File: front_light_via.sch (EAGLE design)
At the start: 9 parts

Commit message: via gerbers generated
via boards completed and gerbers generated
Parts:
- renumbered ETH1 to FRONT, L_DRIVE to BLINK_R, L_SIG to DRIVING_L, R-DRIVE to BLINK_L, R_SIG to DRIVING_R
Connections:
- net N$2 renamed BLINK_L
- net N$4 renamed BLIINK_R
- net N$6 renamed DRIVING_R
- net N$8 renamed DRIVING_L
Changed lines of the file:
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@@
 <?xml version="1.0" encoding="utf-8"?>
 <!DOCTYPE eagle SYSTEM "eagle.dtd">
-<eagle version="8.3.1">
+<eagle version="8.6.0">
 <drawing>
 <settings>
@@
 </classes>
 <parts>
-<part name="ETH1" library="ETHERNET" deviceset="ETHERNET" device=""/>
-<part name="L_SIG" library="TE 2-pin connector" deviceset="2_PIN_TECONNECTOR" device=""/>
-<part name="R_SIG" library="TE 2-pin connector" deviceset="2_PIN_TECONNECTOR" device=""/>
-<part name="L_DRIVE" library="TE 2-pin connector" deviceset="2_PIN_TECONNECTOR" device=""/>
-<part name="R-DRIVE" library="TE 2-pin connector" deviceset="2_PIN_TECONNECTOR" device=""/>
+<part name="FRONT" library="ETHERNET" deviceset="ETHERNET" device=""/>
+<part name="DRIVING_L" library="TE 2-pin connector" deviceset="2_PIN_TECONNECTOR" device=""/>
+<part name="DRIVING_R" library="TE 2-pin connector" deviceset="2_PIN_TECONNECTOR" device=""/>
+<part name="BLINK_R" library="TE 2-pin connector" deviceset="2_PIN_TECONNECTOR" device=""/>
+<part name="BLINK_L" library="TE 2-pin connector" deviceset="2_PIN_TECONNECTOR" device=""/>
 <part name="H1" library="SparkFun-Electromechanical" deviceset="STAND-OFF" device=""/>
 <part name="H2" library="SparkFun-Electromechanical" deviceset="STAND-OFF" device=""/>
@@
 </plain>
 <instances>
-<instance part="ETH1" gate="G$1" x="48.26" y="68.58" rot="R180"/>
-<instance part="L_SIG" gate="G$1" x="116.84" y="88.9"/>
-<instance part="R_SIG" gate="G$1" x="119.38" y="68.58"/>
-<instance part="L_DRIVE" gate="G$1" x="119.38" y="50.8"/>
-<instance part="R-DRIVE" gate="G$1" x="119.38" y="30.48"/>
+<instance part="FRONT" gate="G$1" x="48.26" y="68.58" rot="R180"/>
+<instance part="DRIVING_L" gate="G$1" x="116.84" y="88.9"/>
+<instance part="DRIVING_R" gate="G$1" x="119.38" y="68.58"/>
+<instance part="BLINK_R" gate="G$1" x="119.38" y="50.8"/>
+<instance part="BLINK_L" gate="G$1" x="119.38" y="30.48"/>
 <instance part="H1" gate="G$1" x="35.56" y="38.1"/>
 <instance part="H2" gate="G$1" x="40.64" y="38.1"/>
@@
 <net name="N$1" class="0">
 <segment>
-<pinref part="ETH1" gate="G$1" pin="1"/>
+<pinref part="FRONT" gate="G$1" pin="1"/>
 <wire x1="53.34" y1="53.34" x2="63.5" y2="53.34" width="0.1524" layer="91"/>
 <wire x1="63.5" y1="53.34" x2="63.5" y2="27.94" width="0.1524" layer="91"/>
 <wire x1="63.5" y1="27.94" x2="114.3" y2="27.94" width="0.1524" layer="91"/>
-<pinref part="R-DRIVE" gate="G$1" pin="V/SIG"/>
-</segment>
-</net>
-<net name="N$2" class="0">
-<segment>
-<pinref part="ETH1" gate="G$1" pin="2"/>
+<pinref part="BLINK_L" gate="G$1" pin="V/SIG"/>
+<label x="81.28" y="27.94" size="1.778" layer="95"/>
+</segment>
+</net>
+<net name="BLINK_L" class="0">
+<segment>
+<pinref part="FRONT" gate="G$1" pin="2"/>
 <wire x1="53.34" y1="55.88" x2="66.04" y2="55.88" width="0.1524" layer="91"/>
 <wire x1="66.04" y1="55.88" x2="66.04" y2="33.02" width="0.1524" layer="91"/>
 <wire x1="66.04" y1="33.02" x2="101.6" y2="33.02" width="0.1524" layer="91"/>
-<pinref part="R-DRIVE" gate="G$1" pin="G/LOW"/>
+<pinref part="BLINK_L" gate="G$1" pin="G/LOW"/>
 <wire x1="101.6" y1="33.02" x2="102.87" y2="33.02" width="0.1524" layer="91"/>
 <wire x1="102.87" y1="33.02" x2="114.3" y2="33.02" width="0.1524" layer="91"/>
+<label x="81.28" y="33.02" size="1.778" layer="95"/>
 </segment>
 </net>
 <net name="N$3" class="0">
 <segment>
-<pinref part="ETH1" gate="G$1" pin="3"/>
+<pinref part="FRONT" gate="G$1" pin="3"/>
 <wire x1="53.34" y1="58.42" x2="71.12" y2="58.42" width="0.1524" layer="91"/>
 <wire x1="71.12" y1="58.42" x2="71.12" y2="48.26" width="0.1524" layer="91"/>
 <wire x1="71.12" y1="48.26" x2="101.6" y2="48.26" width="0.1524" layer="91"/>
-<pinref part="L_DRIVE" gate="G$1" pin="V/SIG"/>
+<pinref part="BLINK_R" gate="G$1" pin="V/SIG"/>
 <wire x1="101.6" y1="48.26" x2="102.87" y2="48.26" width="0.1524" layer="91"/>
 <wire x1="102.87" y1="48.26" x2="114.3" y2="48.26" width="0.1524" layer="91"/>
-</segment>
-</net>
-<net name="N$4" class="0">
-<segment>
-<pinref part="ETH1" gate="G$1" pin="4"/>
+<label x="83.82" y="48.26" size="1.778" layer="95"/>
+</segment>
+</net>
+<net name="BLIINK_R" class="0">
+<segment>
+<pinref part="FRONT" gate="G$1" pin="4"/>
 <wire x1="53.34" y1="60.96" x2="73.66" y2="60.96" width="0.1524" layer="91"/>
 <wire x1="73.66" y1="60.96" x2="73.66" y2="53.34" width="0.1524" layer="91"/>
 <wire x1="73.66" y1="53.34" x2="101.6" y2="53.34" width="0.1524" layer="91"/>
-<pinref part="L_DRIVE" gate="G$1" pin="G/LOW"/>
+<pinref part="BLINK_R" gate="G$1" pin="G/LOW"/>
 <wire x1="101.6" y1="53.34" x2="102.87" y2="53.34" width="0.1524" layer="91"/>
 <wire x1="102.87" y1="53.34" x2="114.3" y2="53.34" width="0.1524" layer="91"/>
+<label x="86.36" y="53.34" size="1.778" layer="95"/>
 </segment>
 </net>
 <net name="N$5" class="0">
 <segment>
-<pinref part="ETH1" gate="G$1" pin="5"/>
+<pinref part="FRONT" gate="G$1" pin="5"/>
 <wire x1="53.34" y1="63.5" x2="101.6" y2="63.5" width="0.1524" layer="91"/>
-<pinref part="R_SIG" gate="G$1" pin="V/SIG"/>
+<pinref part="DRIVING_R" gate="G$1" pin="V/SIG"/>
 <wire x1="101.6" y1="63.5" x2="102.87" y2="63.5" width="0.1524" layer="91"/>
 <wire x1="104.14" y1="63.5" x2="104.14" y2="66.04" width="0.1524" layer="91"/>
 <wire x1="104.14" y1="66.04" x2="114.3" y2="66.04" width="0.1524" layer="91"/>
 <wire x1="102.87" y1="63.5" x2="104.14" y2="63.5" width="0.1524" layer="91"/>
-</segment>
-</net>
-<net name="N$6" class="0">
-<segment>
-<pinref part="ETH1" gate="G$1" pin="6"/>
+<label x="88.9" y="63.5" size="1.778" layer="95"/>
+</segment>
+</net>
+<net name="DRIVING_R" class="0">
+<segment>
+<pinref part="FRONT" gate="G$1" pin="6"/>
 <wire x1="53.34" y1="66.04" x2="96.52" y2="66.04" width="0.1524" layer="91"/>
 <wire x1="96.52" y1="66.04" x2="96.52" y2="71.12" width="0.1524" layer="91"/>
 <wire x1="96.52" y1="71.12" x2="101.6" y2="71.12" width="0.1524" layer="91"/>
-<pinref part="R_SIG" gate="G$1" pin="G/LOW"/>
+<pinref part="DRIVING_R" gate="G$1" pin="G/LOW"/>
 <wire x1="101.6" y1="71.12" x2="102.87" y2="71.12" width="0.1524" layer="91"/>
 <wire x1="102.87" y1="71.12" x2="114.3" y2="71.12" width="0.1524" layer="91"/>
+<label x="86.36" y="66.04" size="1.778" layer="95"/>
 </segment>
 </net>
 <net name="N$7" class="0">
 <segment>
-<pinref part="ETH1" gate="G$1" pin="7"/>
+<pinref part="FRONT" gate="G$1" pin="7"/>
 <wire x1="53.34" y1="68.58" x2="91.44" y2="68.58" width="0.1524" layer="91"/>
 <wire x1="91.44" y1="68.58" x2="91.44" y2="86.36" width="0.1524" layer="91"/>
-<pinref part="L_SIG" gate="G$1" pin="V/SIG"/>
+<pinref part="DRIVING_L" gate="G$1" pin="V/SIG"/>
 <wire x1="111.76" y1="86.36" x2="91.44" y2="86.36" width="0.1524" layer="91"/>
-</segment>
-</net>
-<net name="N$8" class="0">
-<segment>
-<pinref part="ETH1" gate="G$1" pin="8"/>
+<label x="81.28" y="68.58" size="1.778" layer="95"/>
+</segment>
+</net>
+<net name="DRIVING_L" class="0">
+<segment>
+<pinref part="FRONT" gate="G$1" pin="8"/>
 <wire x1="53.34" y1="71.12" x2="86.36" y2="71.12" width="0.1524" layer="91"/>
-<pinref part="L_SIG" gate="G$1" pin="G/LOW"/>
+<pinref part="DRIVING_L" gate="G$1" pin="G/LOW"/>
 <wire x1="86.36" y1="71.12" x2="86.36" y2="91.44" width="0.1524" layer="91"/>
 <wire x1="86.36" y1="91.44" x2="111.76" y2="91.44" width="0.1524" layer="91"/>
-</segment>
-</net>
+<label x="76.2" y="71.12" size="1.778" layer="95"/>
+</segment>
+</net>

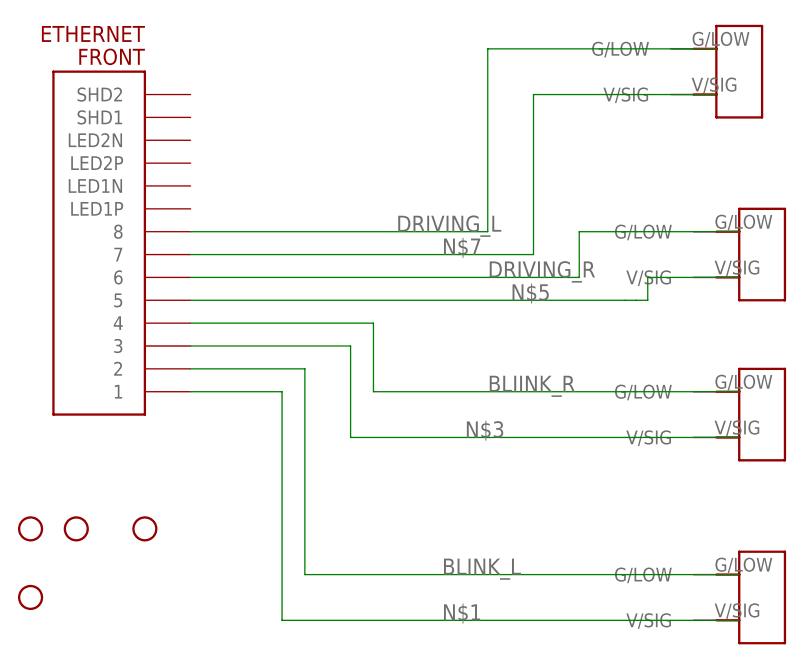
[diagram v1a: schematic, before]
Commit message: added reverse polairity protection
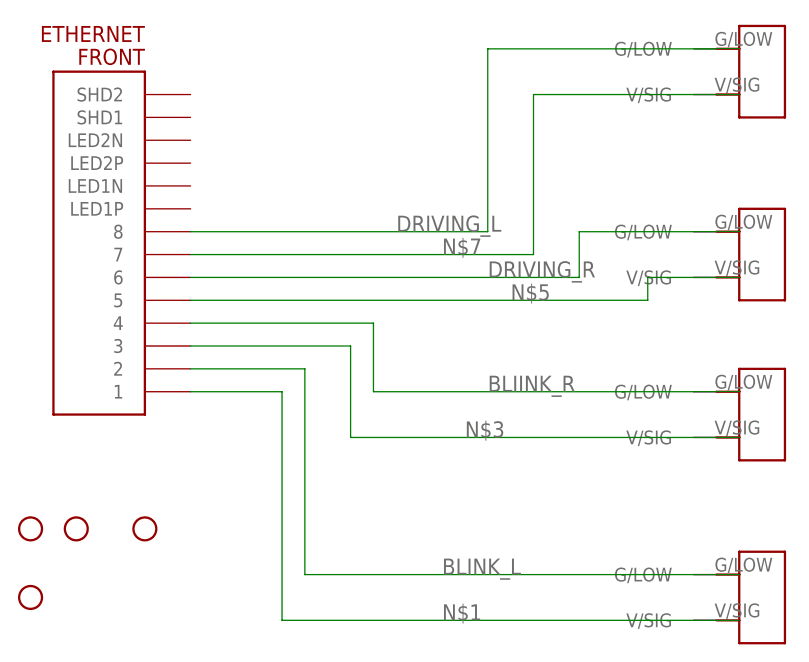
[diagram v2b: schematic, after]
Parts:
- removed DRIVING_L: 2_PIN_TECONNECTOR, TE 2-pin connector:2_PIN_TECONNECTOR
- added U$1: 2_PIN_TECONNECTOR, TE 2-pin connector:2_PIN_TECONNECTOR
- renumbered BLINK_L to U$4, BLINK_R to U$3, DRIVING_R to U$2
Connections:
- net DRIVING_L: now also U$1.G/LOW; no longer DRIVING_L.G/LOW
- net N$7: now also U$1.V/SIG; no longer DRIVING_L.V/SIG
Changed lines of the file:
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@@
 <?xml version="1.0" encoding="utf-8"?>
 <!DOCTYPE eagle SYSTEM "eagle.dtd">
-<eagle version="8.6.0">
+<eagle version="8.6.1">
 <drawing>
 <settings>
@@
 <parts>
 <part name="FRONT" library="ETHERNET" deviceset="ETHERNET" device=""/>
-<part name="DRIVING_L" library="TE 2-pin connector" deviceset="2_PIN_TECONNECTOR" device=""/>
-<part name="DRIVING_R" library="TE 2-pin connector" deviceset="2_PIN_TECONNECTOR" device=""/>
-<part name="BLINK_R" library="TE 2-pin connector" deviceset="2_PIN_TECONNECTOR" device=""/>
-<part name="BLINK_L" library="TE 2-pin connector" deviceset="2_PIN_TECONNECTOR" device=""/>
 <part name="H1" library="SparkFun-Electromechanical" deviceset="STAND-OFF" device=""/>
 <part name="H2" library="SparkFun-Electromechanical" deviceset="STAND-OFF" device=""/>
 <part name="H3" library="SparkFun-Electromechanical" deviceset="STAND-OFF" device=""/>
 <part name="H4" library="SparkFun-Electromechanical" deviceset="STAND-OFF" device=""/>
+<part name="U$1" library="TE 2-pin connector" deviceset="2_PIN_TECONNECTOR" device=""/>
+<part name="U$2" library="TE 2-pin connector" deviceset="2_PIN_TECONNECTOR" device=""/>
+<part name="U$3" library="TE 2-pin connector" deviceset="2_PIN_TECONNECTOR" device=""/>
+<part name="U$4" library="TE 2-pin connector" deviceset="2_PIN_TECONNECTOR" device=""/>
 </parts>
 <sheets>
@@
 <instances>
 <instance part="FRONT" gate="G$1" x="48.26" y="68.58" rot="R180"/>
-<instance part="DRIVING_L" gate="G$1" x="116.84" y="88.9"/>
-<instance part="DRIVING_R" gate="G$1" x="119.38" y="68.58"/>
-<instance part="BLINK_R" gate="G$1" x="119.38" y="50.8"/>
-<instance part="BLINK_L" gate="G$1" x="119.38" y="30.48"/>
 <instance part="H1" gate="G$1" x="35.56" y="38.1"/>
 <instance part="H2" gate="G$1" x="40.64" y="38.1"/>
 <instance part="H3" gate="G$1" x="48.26" y="38.1"/>
 <instance part="H4" gate="G$1" x="35.56" y="30.48"/>
+<instance part="U$1" gate="G$1" x="119.38" y="88.9"/>
+<instance part="U$2" gate="G$1" x="119.38" y="68.58"/>
+<instance part="U$3" gate="G$1" x="119.38" y="50.8"/>
+<instance part="U$4" gate="G$1" x="119.38" y="30.48"/>
 </instances>
 <busses>
@@
 <wire x1="63.5" y1="53.34" x2="63.5" y2="27.94" width="0.1524" layer="91"/>
 <wire x1="63.5" y1="27.94" x2="114.3" y2="27.94" width="0.1524" layer="91"/>
-<pinref part="BLINK_L" gate="G$1" pin="V/SIG"/>
 <label x="81.28" y="27.94" size="1.778" layer="95"/>
+<pinref part="U$4" gate="G$1" pin="V/SIG"/>
 </segment>
 </net>
@@
 <wire x1="53.34" y1="55.88" x2="66.04" y2="55.88" width="0.1524" layer="91"/>
 <wire x1="66.04" y1="55.88" x2="66.04" y2="33.02" width="0.1524" layer="91"/>
-<wire x1="66.04" y1="33.02" x2="101.6" y2="33.02" width="0.1524" layer="91"/>
-<pinref part="BLINK_L" gate="G$1" pin="G/LOW"/>
-<wire x1="101.6" y1="33.02" x2="102.87" y2="33.02" width="0.1524" layer="91"/>
-<wire x1="102.87" y1="33.02" x2="114.3" y2="33.02" width="0.1524" layer="91"/>
+<wire x1="66.04" y1="33.02" x2="114.3" y2="33.02" width="0.1524" layer="91"/>
 <label x="81.28" y="33.02" size="1.778" layer="95"/>
+<pinref part="U$4" gate="G$1" pin="G/LOW"/>
 </segment>
 </net>
@@
 <wire x1="53.34" y1="58.42" x2="71.12" y2="58.42" width="0.1524" layer="91"/>
 <wire x1="71.12" y1="58.42" x2="71.12" y2="48.26" width="0.1524" layer="91"/>
-<wire x1="71.12" y1="48.26" x2="101.6" y2="48.26" width="0.1524" layer="91"/>
-<pinref part="BLINK_R" gate="G$1" pin="V/SIG"/>
-<wire x1="101.6" y1="48.26" x2="102.87" y2="48.26" width="0.1524" layer="91"/>
-<wire x1="102.87" y1="48.26" x2="114.3" y2="48.26" width="0.1524" layer="91"/>
+<wire x1="71.12" y1="48.26" x2="114.3" y2="48.26" width="0.1524" layer="91"/>
 <label x="83.82" y="48.26" size="1.778" layer="95"/>
+<pinref part="U$3" gate="G$1" pin="V/SIG"/>
 </segment>
 </net>
@@
 <wire x1="53.34" y1="60.96" x2="73.66" y2="60.96" width="0.1524" layer="91"/>
 <wire x1="73.66" y1="60.96" x2="73.66" y2="53.34" width="0.1524" layer="91"/>
-<wire x1="73.66" y1="53.34" x2="101.6" y2="53.34" width="0.1524" layer="91"/>
-<pinref part="BLINK_R" gate="G$1" pin="G/LOW"/>
-<wire x1="101.6" y1="53.34" x2="102.87" y2="53.34" width="0.1524" layer="91"/>
-<wire x1="102.87" y1="53.34" x2="114.3" y2="53.34" width="0.1524" layer="91"/>
+<wire x1="73.66" y1="53.34" x2="114.3" y2="53.34" width="0.1524" layer="91"/>
 <label x="86.36" y="53.34" size="1.778" layer="95"/>
+<pinref part="U$3" gate="G$1" pin="G/LOW"/>
 </segment>
 </net>
@@
 <segment>
 <pinref part="FRONT" gate="G$1" pin="5"/>
-<wire x1="53.34" y1="63.5" x2="101.6" y2="63.5" width="0.1524" layer="91"/>
-<pinref part="DRIVING_R" gate="G$1" pin="V/SIG"/>
-<wire x1="101.6" y1="63.5" x2="102.87" y2="63.5" width="0.1524" layer="91"/>
+<wire x1="53.34" y1="63.5" x2="104.14" y2="63.5" width="0.1524" layer="91"/>
 <wire x1="104.14" y1="63.5" x2="104.14" y2="66.04" width="0.1524" layer="91"/>
 <wire x1="104.14" y1="66.04" x2="114.3" y2="66.04" width="0.1524" layer="91"/>
-<wire x1="102.87" y1="63.5" x2="104.14" y2="63.5" width="0.1524" layer="91"/>
 <label x="88.9" y="63.5" size="1.778" layer="95"/>
+<pinref part="U$2" gate="G$1" pin="V/SIG"/>
 </segment>
 </net>
@@
 <wire x1="53.34" y1="66.04" x2="96.52" y2="66.04" width="0.1524" layer="91"/>
 <wire x1="96.52" y1="66.04" x2="96.52" y2="71.12" width="0.1524" layer="91"/>
-<wire x1="96.52" y1="71.12" x2="101.6" y2="71.12" width="0.1524" layer="91"/>
-<pinref part="DRIVING_R" gate="G$1" pin="G/LOW"/>
-<wire x1="101.6" y1="71.12" x2="102.87" y2="71.12" width="0.1524" layer="91"/>
-<wire x1="102.87" y1="71.12" x2="114.3" y2="71.12" width="0.1524" layer="91"/>
+<wire x1="96.52" y1="71.12" x2="114.3" y2="71.12" width="0.1524" layer="91"/>
 <label x="86.36" y="66.04" size="1.778" layer="95"/>
+<pinref part="U$2" gate="G$1" pin="G/LOW"/>
 </segment>
 </net>
@@
 <wire x1="53.34" y1="68.58" x2="91.44" y2="68.58" width="0.1524" layer="91"/>
 <wire x1="91.44" y1="68.58" x2="91.44" y2="86.36" width="0.1524" layer="91"/>
-<pinref part="DRIVING_L" gate="G$1" pin="V/SIG"/>
-<wire x1="111.76" y1="86.36" x2="91.44" y2="86.36" width="0.1524" layer="91"/>
+<wire x1="114.3" y1="86.36" x2="91.44" y2="86.36" width="0.1524" layer="91"/>
 <label x="81.28" y="68.58" size="1.778" layer="95"/>
+<pinref part="U$1" gate="G$1" pin="V/SIG"/>
 </segment>
 </net>
@@
 <pinref part="FRONT" gate="G$1" pin="8"/>
 <wire x1="53.34" y1="71.12" x2="86.36" y2="71.12" width="0.1524" layer="91"/>
-<pinref part="DRIVING_L" gate="G$1" pin="G/LOW"/>
 <wire x1="86.36" y1="71.12" x2="86.36" y2="91.44" width="0.1524" layer="91"/>
-<wire x1="86.36" y1="91.44" x2="111.76" y2="91.44" width="0.1524" layer="91"/>
+<wire x1="86.36" y1="91.44" x2="114.3" y2="91.44" width="0.1524" layer="91"/>
 <label x="76.2" y="71.12" size="1.778" layer="95"/>
-</segment>
-</net>
+<pinref part="U$1" gate="G$1" pin="G/LOW"/>
+</segment>
+</net>
